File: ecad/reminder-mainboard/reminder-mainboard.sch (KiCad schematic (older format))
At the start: 24 parts, among them J1 USB_B_Micro, J2 Conn_01x03_Male, J4 22-03-5065, J5 MOLEX SL 1x5, Q1 2N3904, SW1 SW_SPDT, SW2 SW_Push, SW3 SW_Push, U1 LM1117-3.3, U2 QRD1113GR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

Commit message: Broke out file structure for separate boards
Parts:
- removed C7: 4.7uF, Capacitor_THT:CP_Radial_D4.0mm_P1.50mm, symbol Device:CP1_Small
- added C5: 100nF, Capacitor_SMD:C_0805_2012Metric, symbol Device:C_Small
- added C6: 10uF, Capacitor_Tantalum_SMD:CP_EIA-6032-28_Kemet-C, symbol Device:C_Small
- BZ1: value (none) -> Buzzer; DNP (none) -> 1
- C1: footprint Capacitor_THT:C_Rect_L7.0mm_W4.5mm_P5.00mm -> Capacitor_Tantalum_SMD:CP_EIA-6032-28_Kemet-C; Mfg (none) -> KEMET; Mfg PN TAP106K016CRW -> T491C106K025AT
- C2: value 10uF -> 100uF; footprint Capacitor_THT:C_Rect_L7.0mm_W4.5mm_P5.00mm -> Capacitor_Tantalum_SMD:CP_EIA-3528-21_Kemet-B; Mfg (none) -> AVX; Mfg PN TAP106K016CRW -> TAJB107K006RNJ
- C3: renamed from C5; footprint Capacitor_THT:C_Rect_L7.0mm_W4.5mm_P5.00mm -> Capacitor_SMD:C_0805_2012Metric; Mfg (none) -> YAGEO; Mfg PN (none) -> CC0805KRX7R9BB104
- C4: renamed from C6; footprint Capacitor_Tantalum_SMD:CP_EIA-3216-10_Kemet-I -> Capacitor_SMD:C_0805_2012Metric; Mfg (none) -> YAGEO; Mfg PN (none) -> CC0805KRX7R9BB104
- J1, J4: DNP (none) -> 1
- J2: renamed from J5; DNP (none) -> 1
- J3: renamed from J2; DNP (none) -> 1
- Q1: footprint Package_TO_SOT_THT:TO-92_Inline -> Package_TO_SOT_SMD:SOT-23; Mfg (none) -> Changjiang Electronics Tech (CJ); Mfg PN (none) -> S8050
- R1: value 620 -> 510; footprint Resistor_THT:R_Axial_DIN0204_L3.6mm_D1.6mm_P5.08mm_Horizontal -> Resistor_SMD:R_0603_1608Metric; Mfg Vishay -> Uniroyal Elec; Mfg PN MBA02040C6200FC100 -> 0603WAF5100T5E
- R2: footprint Resistor_THT:R_Axial_DIN0204_L3.6mm_D1.6mm_P5.08mm_Horizontal -> Resistor_SMD:R_0603_1608Metric; Mfg (none) -> Uniroyal Elec; Mfg PN (none) -> 0603WAF1002T5E
- R3: renamed from R8; footprint Resistor_THT:R_Axial_DIN0204_L3.6mm_D1.6mm_P5.08mm_Horizontal -> Resistor_SMD:R_0603_1608Metric; Mfg (none) -> Uniroyal Elec; Mfg PN (none) -> 0603WAF1002T5E
- R4: renamed from R10; value 180 -> 160; footprint Resistor_THT:R_Axial_DIN0204_L3.6mm_D1.6mm_P5.08mm_Horizontal -> Resistor_SMD:R_0603_1608Metric; Mfg (none) -> Uniroyal Elec; Mfg PN (none) -> 0603WAF1600T5E
- R5: renamed from R12; footprint Resistor_THT:R_Axial_DIN0204_L3.6mm_D1.6mm_P5.08mm_Horizontal -> Resistor_SMD:R_0603_1608Metric; Mfg (none) -> Uniroyal Elec; Mfg PN (none) -> 0603WAF1002T5E
- R6: renamed from R3; footprint Resistor_THT:R_Axial_DIN0204_L3.6mm_D1.6mm_P5.08mm_Horizontal -> Resistor_SMD:R_0603_1608Metric; Mfg (none) -> Uniroyal Elec; Mfg PN (none) -> 0603WAF1002T5E
- R7: renamed from R13; footprint Resistor_THT:R_Axial_DIN0204_L3.6mm_D1.6mm_P5.08mm_Horizontal -> Resistor_SMD:R_0603_1608Metric; Mfg (none) -> Uniroyal Elec; Mfg PN (none) -> 0603WAF1002T5E
- U1: footprint Package_TO_SOT_THT:TO-220-3_Vertical -> Package_TO_SOT_SMD:SOT-223-3_TabPin2; Mfg (none) -> Texas Instruments; Mfg PN (none) -> LM1117IMPX-3.3/NOPB
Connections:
- wire segments 98 -> 100

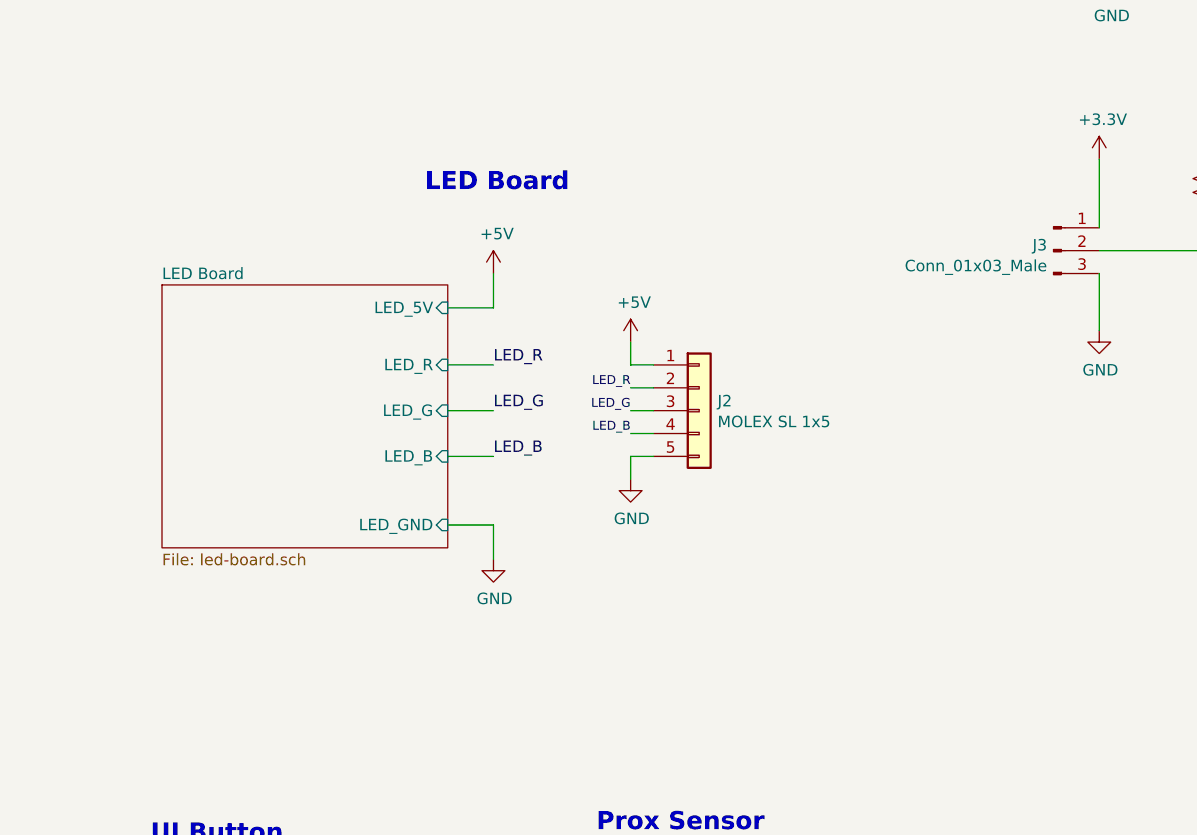
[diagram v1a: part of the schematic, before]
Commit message: Began SMD layout
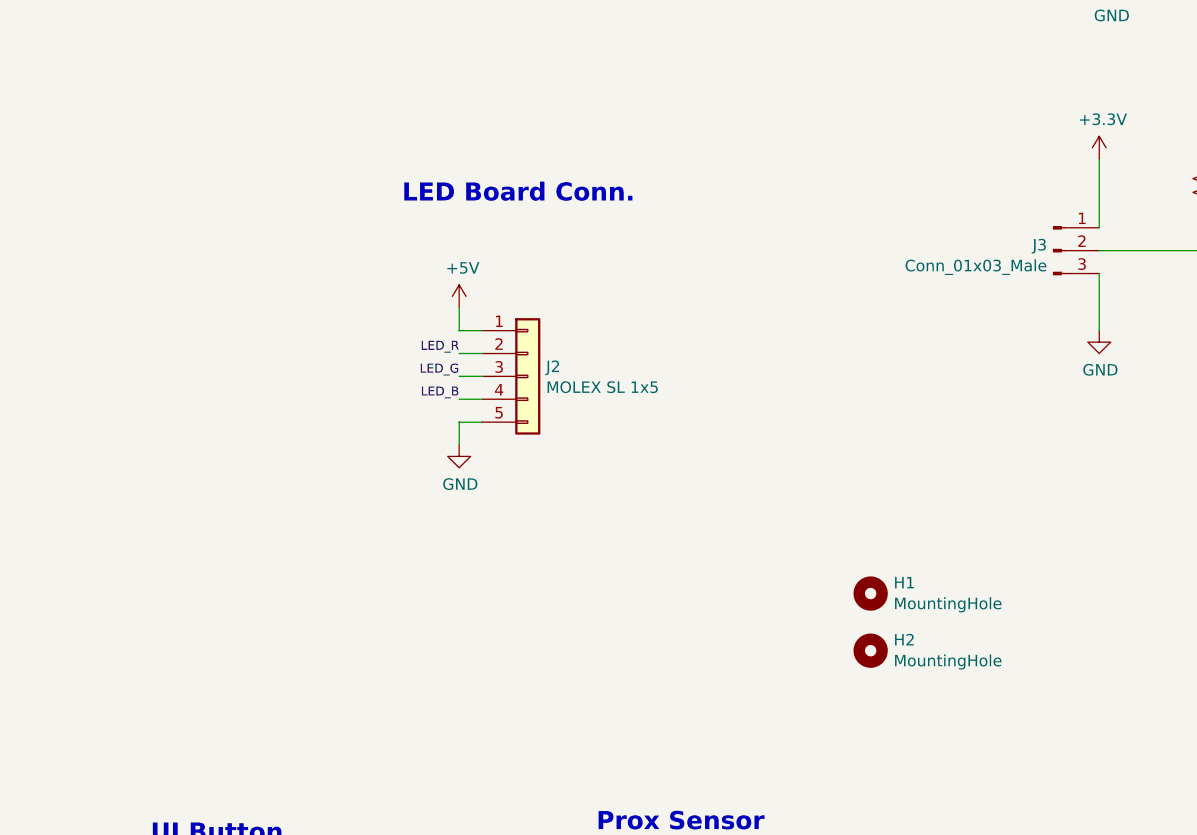
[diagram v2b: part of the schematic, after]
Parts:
- added H1, H2: MountingHole, MountingHole:MountingHole_2.7mm_M2.5_Pad, symbol Mechanical:MountingHole
- C6: footprint Capacitor_Tantalum_SMD:CP_EIA-6032-28_Kemet-C -> Capacitor_Tantalum_SMD:CP_EIA-3528-21_Kemet-B; Mfg KEMET -> AVX; Mfg PN T491C106K025AT -> TAJB106M025RNJ
- J3: footprint (none) -> Connector_PinHeader_2.54mm:PinHeader_1x03_P2.54mm_Vertical
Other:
- note added: "LED Board Conn.\n"
- note removed: "LED Board"
- moved on the sheet: J2
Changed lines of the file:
@@
 $Descr A4 11693 8268
 encoding utf-8
-Sheet 1 2
+Sheet 1 1
 Title ""
 Date ""
@@
 $EndComp
 $Comp
-L power:GND #PWR017
+L power:GND #PWR015
 U 1 1 608AF457
 P 5450 7100
-F 0 "#PWR017" H 5450 6850 50  0001 C CNN
+F 0 "#PWR015" H 5450 6850 50  0001 C CNN
 F 1 "GND" H 5455 6927 50  0000 C CNN
 F 2 "" H 5450 7100 50  0001 C CNN
@@
 $EndComp
 $Comp
-L power:+3.3V #PWR019
+L power:+3.3V #PWR017
 U 1 1 608AE420
 P 6200 6400
-F 0 "#PWR019" H 6200 6250 50  0001 C CNN
+F 0 "#PWR017" H 6200 6250 50  0001 C CNN
 F 1 "+3.3V" H 6215 6573 50  0000 C CNN
 F 2 "" H 6200 6400 50  0001 C CNN
@@
 $EndComp
 $Comp
-L power:GND #PWR018
+L power:GND #PWR016
 U 1 1 608ADD02
 P 6050 7100
-F 0 "#PWR018" H 6050 6850 50  0001 C CNN
+F 0 "#PWR016" H 6050 6850 50  0001 C CNN
 F 1 "GND" H 6055 6927 50  0000 C CNN
 F 2 "" H 6050 7100 50  0001 C CNN
@@
 NRST
 $Comp
-L power:GND #PWR028
+L power:GND #PWR026
 U 1 1 60875A5D
 P 8850 5750
-F 0 "#PWR028" H 8850 5500 50  0001 C CNN
+F 0 "#PWR026" H 8850 5500 50  0001 C CNN
 F 1 "GND" H 8855 5577 50  0000 C CNN
 F 2 "" H 8850 5750 50  0001 C CNN
@@
 $EndComp
 $Comp
-L power:+3.3V #PWR027
+L power:+3.3V #PWR025
 U 1 1 608750FB
 P 8850 4900
-F 0 "#PWR027" H 8850 4750 50  0001 C CNN
+F 0 "#PWR025" H 8850 4750 50  0001 C CNN
 F 1 "+3.3V" H 8865 5073 50  0000 C CNN
 F 2 "" H 8850 4900 50  0001 C CNN
@@
 NoConn ~ 9550 1850
 $Comp
-L power:GND #PWR026
+L power:GND #PWR024
 U 1 1 605DDA1D
 P 8750 3150
-F 0 "#PWR026" H 8750 2900 50  0001 C CNN
+F 0 "#PWR024" H 8750 2900 50  0001 C CNN
 F 1 "GND" H 8755 2977 50  0000 C CNN
 F 2 "" H 8750 3150 50  0001 C CNN
@@
 	8350 1850 7850 1850
 $Comp
-L power:GND #PWR022
+L power:GND #PWR020
 U 1 1 605C84C2
 P 7500 2250
-F 0 "#PWR022" H 7500 2000 50  0001 C CNN
+F 0 "#PWR020" H 7500 2000 50  0001 C CNN
 F 1 "GND" H 7505 2077 50  0000 C CNN
 F 2 "" H 7500 2250 50  0001 C CNN
@@
 $EndComp
 $Comp
-L power:GND #PWR024
+L power:GND #PWR022
 U 1 1 605BD8D9
 P 7850 2150
-F 0 "#PWR024" H 7850 1900 50  0001 C CNN
+F 0 "#PWR022" H 7850 1900 50  0001 C CNN
 F 1 "GND" H 7855 1977 50  0000 C CNN
 F 2 "" H 7850 2150 50  0001 C CNN
@@
 $EndComp
 $Comp
-L power:+3.3V #PWR020
+L power:+3.3V #PWR018
 U 1 1 605A71FA
 P 7450 3050
-F 0 "#PWR020" H 7450 2900 50  0001 C CNN
+F 0 "#PWR018" H 7450 2900 50  0001 C CNN
 F 1 "+3.3V" H 7465 3223 50  0000 C CNN
 F 2 "" H 7450 3050 50  0001 C CNN
@@
 $EndComp
 $Comp
-L power:GND #PWR021
+L power:GND #PWR019
 U 1 1 605A6B9F
 P 7450 3800
-F 0 "#PWR021" H 7450 3550 50  0001 C CNN
+F 0 "#PWR019" H 7450 3550 50  0001 C CNN
 F 1 "GND" H 7455 3627 50  0000 C CNN
 F 2 "" H 7450 3800 50  0001 C CNN
@@
 Connection ~ 8750 1400
 $Comp
-L power:+3.3V #PWR025
+L power:+3.3V #PWR023
 U 1 1 605677FC
 P 8750 1350
-F 0 "#PWR025" H 8750 1200 50  0001 C CNN
+F 0 "#PWR023" H 8750 1200 50  0001 C CNN
 F 1 "+3.3V" H 8765 1523 50  0000 C CNN
 F 2 "" H 8750 1350 50  0001 C CNN
@@
 $EndComp
 $Comp
-L power:GND #PWR029
+L power:GND #PWR027
 U 1 1 6056EBB5
 P 10000 1650
-F 0 "#PWR029" H 10000 1400 50  0001 C CNN
+F 0 "#PWR027" H 10000 1400 50  0001 C CNN
 F 1 "GND" H 10005 1477 50  0000 C CNN
 F 2 "" H 10000 1650 50  0001 C CNN
@@
 $EndComp
 $Comp
-L power:+3.3V #PWR023
+L power:+3.3V #PWR021
 U 1 1 6077ABD6
 P 7850 1550
-F 0 "#PWR023" H 7850 1400 50  0001 C CNN
+F 0 "#PWR021" H 7850 1400 50  0001 C CNN
 F 1 "+3.3V" H 7865 1723 50  0000 C CNN
 F 2 "" H 7850 1550 50  0001 C CNN
@@
 F 0 "J3" H 7222 3474 50  0000 R CNN
 F 1 "Conn_01x03_Male" H 7222 3383 50  0000 R CNN
-F 2 "" H 7250 3450 50  0001 C CNN
+F 2 "Connector_PinHeader_2.54mm:PinHeader_1x03_P2.54mm_Vertical" H 7250 3450 50  0001 C CNN
 F 3 "~" H 7250 3450 50  0001 C CNN
 F 4 "1" H 7250 3450 50  0001 C CNN "DNP"
@@
 Wire Wire Line
 	7450 3450 7900 3450
+Wire Wire Line
+	4650 4200 4750 4200
+Wire Wire Line
+	4650 4300 4650 4200
+Wire Wire Line
+	4650 4100 4750 4100
+Wire Wire Line
+	4650 4000 4750 4000
+Wire Wire Line
+	4650 3900 4750 3900
+Wire Wire Line
+	4650 3800 4650 3700
+Wire Wire Line
+	4750 3800 4650 3800
 $Comp
 L power:GND #PWR013
-U 1 1 60820310
-P 4800 4800
-F 0 "#PWR013" H 4800 4550 50  0001 C CNN
-F 1 "GND" H 4805 4627 50  0000 C CNN
-F 2 "" H 4800 4800 50  0001 C CNN
-F 3 "" H 4800 4800 50  0001 C CNN
-	1    4800 4800
-	1    0    0    -1
-$EndComp
-Wire Wire Line
-	5400 4350 5500 4350
-Wire Wire Line
-	5400 4450 5400 4350
-Wire Wire Line
-	5400 4250 5500 4250
-Wire Wire Line
-	5400 4150 5500 4150
-Wire Wire Line
-	5400 4050 5500 4050
-Wire Wire Line
-	5400 3950 5400 3850
-Wire Wire Line
-	5500 3950 5400 3950
-$Comp
-L power:GND #PWR016
 U 1 1 6083AA28
-P 5400 4450
-AR Path="/6083AA28" Ref="#PWR016"  Part="1"
+P 4650 4300
+AR Path="/6083AA28" Ref="#PWR013"  Part="1"
 AR Path="/60793C3B/6083AA28" Ref="#PWR?"  Part="1"
-F 0 "#PWR016" H 5400 4200 50  0001 C CNN
-F 1 "GND" H 5405 4277 50  0000 C CNN
-F 2 "" H 5400 4450 50  0001 C CNN
-F 3 "" H 5400 4450 50  0001 C CNN
-	1    5400 4450
-	1    0    0    -1
-$EndComp
-$Comp
-L power:+5V #PWR015
+F 0 "#PWR013" H 4650 4050 50  0001 C CNN
+F 1 "GND" H 4655 4127 50  0000 C CNN
+F 2 "" H 4650 4300 50  0001 C CNN
+F 3 "" H 4650 4300 50  0001 C CNN
+	1    4650 4300
+	1    0    0    -1
+$EndComp
+$Comp
+L power:+5V #PWR012
 U 1 1 6083AA22
-P 5400 3850
-AR Path="/6083AA22" Ref="#PWR015"  Part="1"
+P 4650 3700
+AR Path="/6083AA22" Ref="#PWR012"  Part="1"
 AR Path="/60793C3B/6083AA22" Ref="#PWR?"  Part="1"
-F 0 "#PWR015" H 5400 3700 50  0001 C CNN
-F 1 "+5V" H 5415 4023 50  0000 C CNN
-F 2 "" H 5400 3850 50  0001 C CNN
-F 3 "" H 5400 3850 50  0001 C CNN
-	1    5400 3850
-	1    0    0    -1
-$EndComp
-Text Label 5400 4050 2    39   ~ 0
+F 0 "#PWR012" H 4650 3550 50  0001 C CNN
+F 1 "+5V" H 4665 3873 50  0000 C CNN
+F 2 "" H 4650 3700 50  0001 C CNN
+F 3 "" H 4650 3700 50  0001 C CNN
+	1    4650 3700
+	1    0    0    -1
+$EndComp
+Text Label 4650 3900 2    39   ~ 0
 LED_R
-Text Label 5400 4150 2    39   ~ 0
+Text Label 4650 4000 2    39   ~ 0
 LED_G
-Text Label 5400 4250 2    39   ~ 0
+Text Label 4650 4100 2    39   ~ 0
 LED_B
 $Comp
 L Connector_Generic:Conn_01x05 J?
 U 1 1 6083AA19
-P 5700 4150
+P 4950 4000
 AR Path="/60793C3B/6083AA19" Ref="J?"  Part="1"
 AR Path="/6083AA19" Ref="J2"  Part="1"
-F 0 "J2" H 5780 4192 50  0000 L CNN
-F 1 "MOLEX SL 1x5" H 5780 4101 50  0000 L CNN
-F 2 "Connector_Molex:Molex_SL_171971-0005_1x05_P2.54mm_Vertical" H 5700 4150 50  0001 C CNN
-F 3 "~" H 5700 4150 50  0001 C CNN
-F 4 "1" H 5700 4150 50  0001 C CNN "DNP"
-	1    5700 4150
-	1    0    0    -1
-$EndComp
-Wire Wire Line
-	4800 4650 4800 4800
-Wire Wire Line
-	4600 4650 4800 4650
-Wire Wire Line
-	4600 4350 4800 4350
-Wire Wire Line
-	4600 4150 4800 4150
-Wire Wire Line
-	4600 3950 4800 3950
-Wire Wire Line
-	4800 3700 4800 3550
-Wire Wire Line
-	4600 3700 4800 3700
-Text Label 4800 4350 0    50   ~ 0
-LED_B
-Text Label 4800 3950 0    50   ~ 0
-LED_R
-Text Label 4800 4150 0    50   ~ 0
-LED_G
-$Comp
-L power:+5V #PWR012
-U 1 1 6081FB75
-P 4800 3550
-F 0 "#PWR012" H 4800 3400 50  0001 C CNN
-F 1 "+5V" H 4815 3723 50  0000 C CNN
-F 2 "" H 4800 3550 50  0001 C CNN
-F 3 "" H 4800 3550 50  0001 C CNN
-	1    4800 3550
-	1    0    0    -1
-$EndComp
-Text Notes 4500 3200 0    79   ~ 16
-LED Board
-$Sheet
-S 3350 3600 1250 1150
-U 60793C3B
-F0 "LED Board" 50
-F1 "led-board.sch" 50
-F2 "LED_R" I R 4600 3950 50
-F3 "LED_G" I R 4600 4150 50
-F4 "LED_B" I R 4600 4350 50
-F5 "LED_5V" I R 4600 3700 50
-F6 "LED_GND" I R 4600 4650 50
-$EndSheet
+F 0 "J2" H 5030 4042 50  0000 L CNN
+F 1 "MOLEX SL 1x5" H 5030 3951 50  0000 L CNN
+F 2 "Connector_Molex:Molex_SL_171971-0005_1x05_P2.54mm_Vertical" H 4950 4000 50  0001 C CNN
+F 3 "~" H 4950 4000 50  0001 C CNN
+F 4 "1" H 4950 4000 50  0001 C CNN "DNP"
+	1    4950 4000
+	1    0    0    -1
+$EndComp
+Text Notes 4400 3250 0    79   ~ 16
+LED Board Conn.\n
 Wire Wire Line
 	9000 1600 9400 1600
@@
 F 0 "C6" H 9892 1546 50  0000 L CNN
 F 1 "10uF" H 9892 1455 50  0000 L CNN
-F 2 "Capacitor_Tantalum_SMD:CP_EIA-6032-28_Kemet-C" H 9800 1500 50  0001 C CNN
-F 3 "https://datasheet.lcsc.com/szlcsc/KEMET-T491C106K025AT_C116748.pdf" H 9800 1500 50  0001 C CNN
-F 4 "KEMET" H 9800 1500 50  0001 C CNN "Mfg"
-F 5 "T491C106K025AT" H 9800 1500 50  0001 C CNN "Mfg PN"
+F 2 "Capacitor_Tantalum_SMD:CP_EIA-3528-21_Kemet-B" H 9800 1500 50  0001 C CNN
+F 3 "https://datasheet.lcsc.com/szlcsc/AVX-TAJB106M025RNJ_C8018.pdf" H 9800 1500 50  0001 C CNN
+F 4 "AVX" H 9800 1500 50  0001 C CNN "Mfg"
+F 5 "TAJB106M025RNJ" H 9800 1500 50  0001 C CNN "Mfg PN"
 	1    9800 1500
 	1    0    0    -1
@@
 Wire Wire Line
 	9400 1400 9800 1400
+$Comp
+L Mechanical:MountingHole H1
+U 1 1 6052873A
+P 6450 4950
+F 0 "H1" H 6550 4996 50  0000 L CNN
+F 1 "MountingHole" H 6550 4905 50  0000 L CNN
+F 2 "MountingHole:MountingHole_2.7mm_M2.5_Pad" H 6450 4950 50  0001 C CNN
+F 3 "~" H 6450 4950 50  0001 C CNN
+	1    6450 4950
+	1    0    0    -1
+$EndComp
+$Comp
+L Mechanical:MountingHole H2
+U 1 1 60528D25
+P 6450 5200
+F 0 "H2" H 6550 5246 50  0000 L CNN
+F 1 "MountingHole" H 6550 5155 50  0000 L CNN
+F 2 "MountingHole:MountingHole_2.7mm_M2.5_Pad" H 6450 5200 50  0001 C CNN
+F 3 "~" H 6450 5200 50  0001 C CNN
+	1    6450 5200
+	1    0    0    -1
+$EndComp
 $EndSCHEMATC
